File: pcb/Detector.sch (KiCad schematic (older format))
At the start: 13 parts, among them U3 AD8310

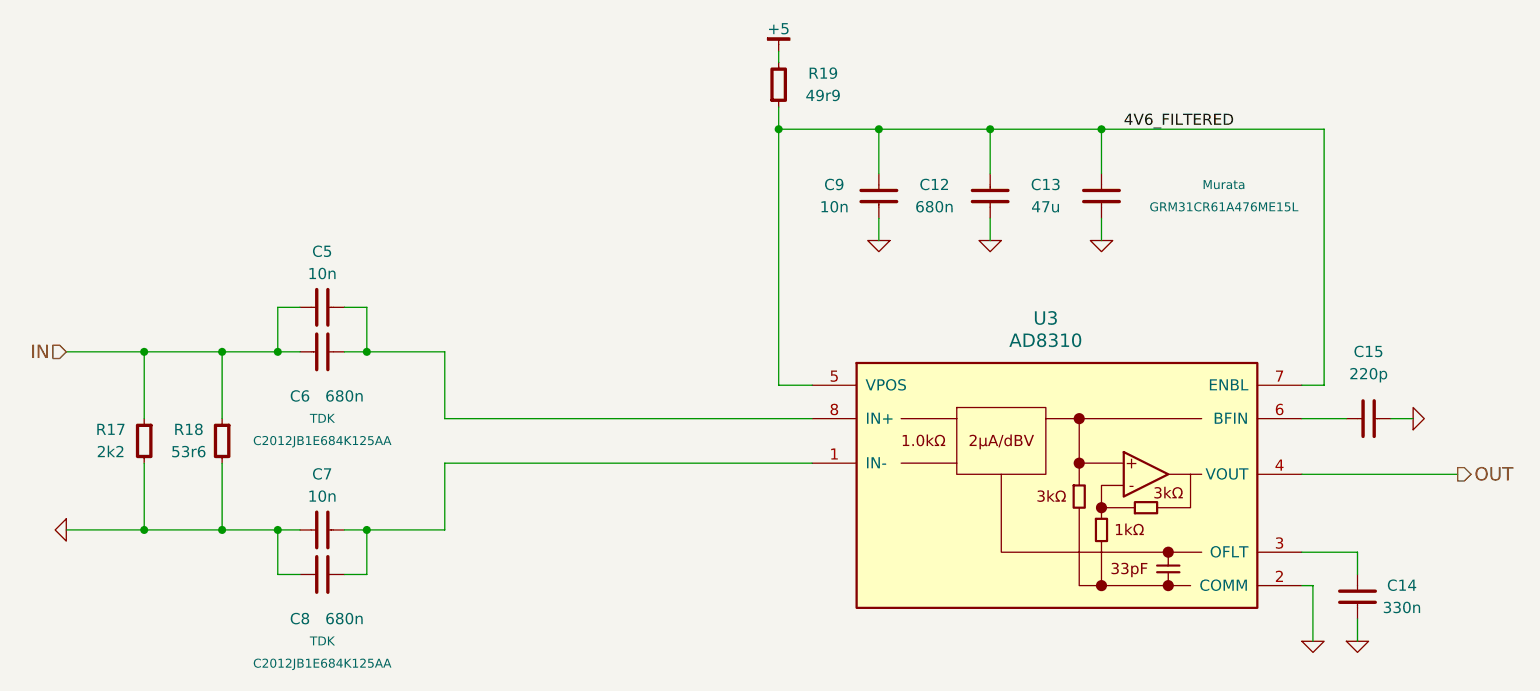
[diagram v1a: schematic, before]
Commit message: Specified part for C14
U# (AD8310) offset filter capacitor
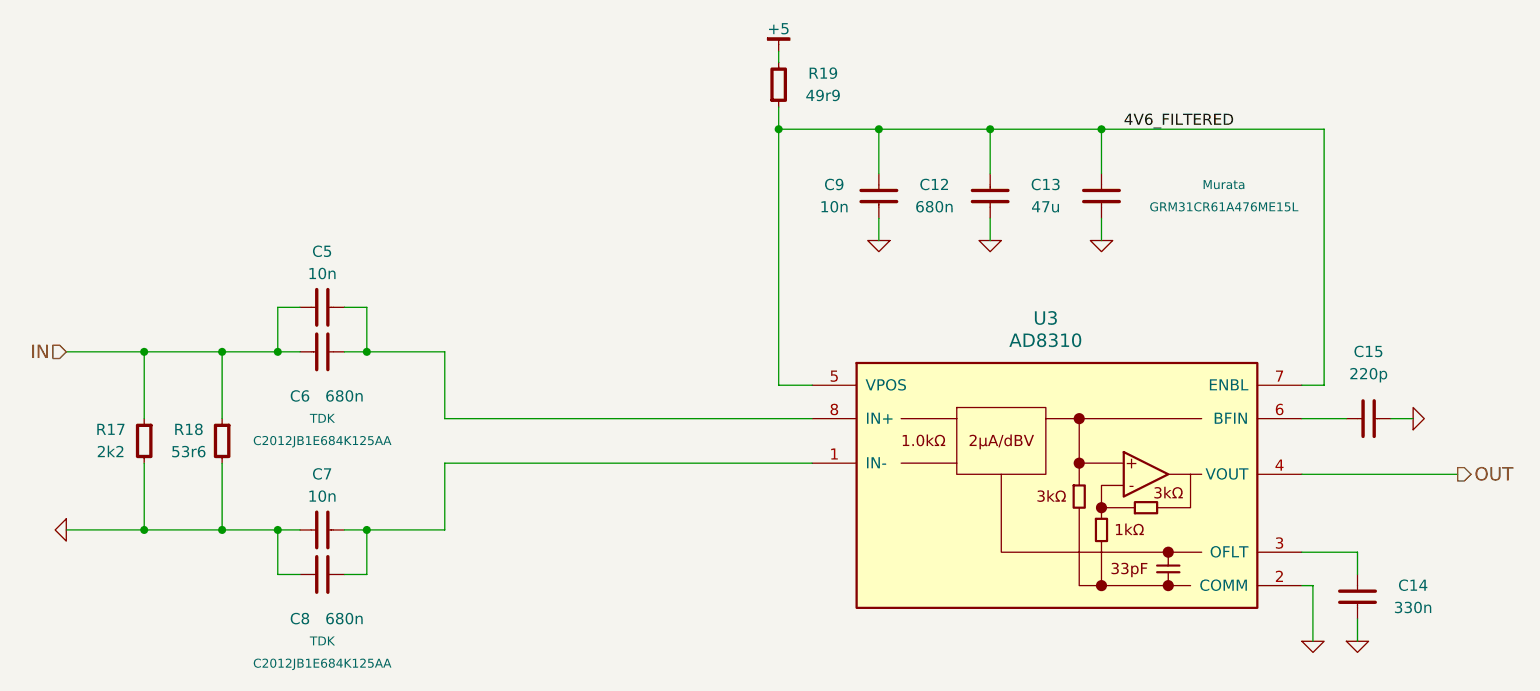
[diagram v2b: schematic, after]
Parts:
- removed C14: 330n, symbol C
- added C14: 330n, symbol C-0603
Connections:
- net GND: now also C14.2
- net at U3.3 (OFLT): now also C14.1
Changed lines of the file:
@@
-$EndComp
-$Comp
-L C C14
-U 1 1 545ED71F
-P 8350 4800
-F 0 "C14" H 8550 4850 50  0000 C CNN
-F 1 "330n" H 8550 4750 50  0000 C CNN
-F 2 "" H 8340 4775 60  0000 C CNN
-F 3 "" H 8340 4775 60  0000 C CNN
-	1    8350 4800
-	1    0    0    -1
 $EndComp
 $Comp
@@
 $EndComp
 $Comp
-L GND #PWR41
+L GND #PWR036
 U 1 1 545ED74D
 P 8150 5000
-F 0 "#PWR41" H 8150 5000 30  0001 C CNN
+F 0 "#PWR036" H 8150 5000 30  0001 C CNN
 F 1 "GND" H 8150 4930 30  0001 C CNN
 F 2 "" H 8150 5000 60  0000 C CNN
@@
 $EndComp
 $Comp
-L GND #PWR42
+L GND #PWR037
 U 1 1 545ED753
 P 8350 5000
-F 0 "#PWR42" H 8350 5000 30  0001 C CNN
+F 0 "#PWR037" H 8350 5000 30  0001 C CNN
 F 1 "GND" H 8350 4930 30  0001 C CNN
 F 2 "" H 8350 5000 60  0000 C CNN
@@
 $EndComp
 $Comp
-L GND #PWR43
+L GND #PWR038
 U 1 1 545ED759
 P 8600 4000
-F 0 "#PWR43" H 8600 4000 30  0001 C CNN
+F 0 "#PWR038" H 8600 4000 30  0001 C CNN
 F 1 "GND" H 8600 3930 30  0001 C CNN
 F 2 "" H 8600 4000 60  0000 C CNN
@@
 	3600 3500 3500 3500
 Wire Wire Line
-	3500 3700 3500 3500
+	3500 3500 3500 3700
 Connection ~ 3500 3700
 Wire Wire Line
@@
 Connection ~ 6700 2700
 $Comp
-L GND #PWR38
+L GND #PWR039
 U 1 1 545ED79D
 P 6200 3200
-F 0 "#PWR38" H 6200 3200 30  0001 C CNN
+F 0 "#PWR039" H 6200 3200 30  0001 C CNN
 F 1 "GND" H 6200 3130 30  0001 C CNN
 F 2 "" H 6200 3200 60  0000 C CNN
@@
 	6200 3200 6200 3100
 $Comp
-L GND #PWR39
+L GND #PWR040
 U 1 1 545ED7A4
 P 6700 3200
-F 0 "#PWR39" H 6700 3200 30  0001 C CNN
+F 0 "#PWR040" H 6700 3200 30  0001 C CNN
 F 1 "GND" H 6700 3130 30  0001 C CNN
 F 2 "" H 6700 3200 60  0000 C CNN
@@
 $EndComp
 $Comp
-L GND #PWR40
+L GND #PWR041
 U 1 1 545ED7C0
 P 7200 3200
-F 0 "#PWR40" H 7200 3200 30  0001 C CNN
+F 0 "#PWR041" H 7200 3200 30  0001 C CNN
 F 1 "GND" H 7200 3130 30  0001 C CNN
 F 2 "" H 7200 3200 60  0000 C CNN
@@
 	2550 4500 3600 4500
 $Comp
-L GND #PWR36
+L GND #PWR042
 U 1 1 545ED89C
 P 2550 4500
-F 0 "#PWR36" H 2550 4500 30  0001 C CNN
+F 0 "#PWR042" H 2550 4500 30  0001 C CNN
 F 1 "GND" H 2550 4430 30  0001 C CNN
 F 2 "" H 2550 4500 60  0000 C CNN
@@
 IN
 $Comp
-L +5 #PWR37
+L +5 #PWR043
 U 1 1 545EDBEE
 P 5750 2350
-F 0 "#PWR37" H 5750 2400 30  0001 C CNN
+F 0 "#PWR043" H 5750 2400 30  0001 C CNN
 F 1 "+5" H 5750 2450 50  0000 C CNN
 F 2 "" H 5750 2350 60  0000 C CNN
@@
 Wire Wire Line
 	4250 4000 4250 3700
+$Comp
+L C-0603 C14
+U 1 1 545FC255
+P 8350 4800
+F 0 "C14" H 8600 4850 50  0000 C CNN
+F 1 "330n" H 8600 4750 50  0000 C CNN
+F 2 "" H 8340 4775 60  0000 C CNN
+F 3 "" H 8340 4775 60  0000 C CNN
+F 4 "C1608JB1E334K080AC" H 8350 4800 60  0001 C CNN "PN"
+F 5 "TDK" H 8350 4800 60  0001 C CNN "Manuf"
+	1    8350 4800
+	1    0    0    -1
+$EndComp
 $EndSCHEMATC

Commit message: Associated parts with footprints
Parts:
- C12, C6, C8: footprint (none) -> IPC7351-Nominal:CAPC2012X70
- C13: footprint (none) -> IPC7351-Nominal:CAPC3216X70
- C14, C15: footprint (none) -> IPC7351-Nominal:CAPC1608X55
- C5, C7, C9: footprint (none) -> IPC7351-Nominal:CAPC1005X55
- R17, R18, R19: footprint (none) -> IPC7351-Nominal:RESC1005X40
- U3: footprint (none) -> IPC7351-Nominal:SOP65P490X109-8
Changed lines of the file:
@@
 F 0 "U3" H 6950 4950 60  0000 C CNN
 F 1 "AD8310" H 6950 4850 60  0000 C CNN
-F 2 "" H 7050 4400 60  0000 C CNN
+F 2 "IPC7351-Nominal:SOP65P490X109-8" H 7050 4400 60  0001 C CNN
 F 3 "" H 7050 4400 60  0000 C CNN
 	1    6950 4250
@@
 F 0 "C15" V 8700 4000 50  0000 C CNN
 F 1 "220p" V 8600 4000 50  0000 C CNN
-F 2 "" H 8390 3975 60  0000 C CNN
+F 2 "IPC7351-Nominal:CAPC1608X55" H 8390 3975 60  0001 C CNN
 F 3 "" H 8390 3975 60  0000 C CNN
 	1    8400 4000
@@
 F 0 "C6" V 3900 3600 50  0000 C CNN
 F 1 "680n" V 3900 3800 50  0000 C CNN
-F 2 "" H 3690 3675 60  0000 C CNN
+F 2 "IPC7351-Nominal:CAPC2012X70" H 3690 3675 60  0001 C CNN
 F 3 "" H 3690 3675 60  0000 C CNN
 F 4 "C2012JB1E684K125AA" V 4100 3700 40  0000 C CNN "PN"
@@
 F 0 "C5" V 3950 3500 50  0000 C CNN
 F 1 "10n" V 3850 3500 50  0000 C CNN
-F 2 "" H 3690 3475 60  0000 C CNN
+F 2 "IPC7351-Nominal:CAPC1005X55" H 3690 3475 60  0001 C CNN
 F 3 "" H 3690 3475 60  0000 C CNN
 	1    3700 3500
@@
 F 0 "C8" V 3900 4600 50  0000 C CNN
 F 1 "680n" V 3900 4800 50  0000 C CNN
-F 2 "" H 3690 4675 60  0000 C CNN
+F 2 "IPC7351-Nominal:CAPC2012X70" H 3690 4675 60  0001 C CNN
 F 3 "" H 3690 4675 60  0000 C CNN
 F 4 "C2012JB1E684K125AA" V 4100 4700 40  0000 C CNN "PN"
@@
 F 0 "C7" V 3950 4500 50  0000 C CNN
 F 1 "10n" V 3850 4500 50  0000 C CNN
-F 2 "" H 3690 4475 60  0000 C CNN
+F 2 "IPC7351-Nominal:CAPC1005X55" H 3690 4475 60  0001 C CNN
 F 3 "" H 3690 4475 60  0000 C CNN
 	1    3700 4500
@@
 F 0 "R18" H 3400 4150 50  0000 C CNN
 F 1 "53r6" H 3400 4050 50  0000 C CNN
-F 2 "" H 3250 4150 60  0000 C CNN
+F 2 "IPC7351-Nominal:RESC1005X40" H 3250 4150 60  0001 C CNN
 F 3 "" H 3250 4150 60  0000 C CNN
 	1    3250 4100
@@
 F 0 "R19" H 5950 2450 50  0000 C CNN
 F 1 "49r9" H 5950 2550 50  0000 C CNN
-F 2 "" H 5750 2550 60  0000 C CNN
+F 2 "IPC7351-Nominal:RESC1005X40" H 5750 2550 60  0001 C CNN
 F 3 "" H 5750 2550 60  0000 C CNN
 	1    5750 2500
@@
 F 0 "C12" H 6450 2950 50  0000 C CNN
 F 1 "680n" H 6450 3050 50  0000 C CNN
-F 2 "" H 6690 2975 60  0000 C CNN
+F 2 "IPC7351-Nominal:CAPC2012X70" H 6690 2975 60  0001 C CNN
 F 3 "" H 6690 2975 60  0000 C CNN
 F 4 "C2012JB1E684K125AA" V 7100 3000 40  0001 C CNN "PN"
@@
 F 0 "C9" H 6400 3050 50  0000 C CNN
 F 1 "10n" H 6400 2950 50  0000 C CNN
-F 2 "" H 6190 2975 60  0000 C CNN
+F 2 "IPC7351-Nominal:CAPC1005X55" H 6190 2975 60  0001 C CNN
 F 3 "" H 6190 2975 60  0000 C CNN
 	1    6200 3000
@@
 F 0 "R17" H 3050 4150 50  0000 C CNN
 F 1 "2k2" H 3050 4050 50  0000 C CNN
-F 2 "" H 2900 4150 60  0000 C CNN
+F 2 "IPC7351-Nominal:RESC1005X40" H 2900 4150 60  0001 C CNN
 F 3 "" H 2900 4150 60  0000 C CNN
 	1    2900 4100
@@
 F 0 "C13" H 7450 3050 50  0000 C CNN
 F 1 "47u" H 7450 2950 50  0000 C CNN
-F 2 "" H 7190 2975 60  0000 C CNN
+F 2 "IPC7351-Nominal:CAPC3216X70" H 7190 2975 60  0001 C CNN
 F 3 "" H 7190 2975 60  0000 C CNN
 F 4 "GRM31CR61A476ME15L" H 6650 2950 40  0000 C CNN "PN"
@@
 F 0 "C14" H 8600 4850 50  0000 C CNN
 F 1 "330n" H 8600 4750 50  0000 C CNN
-F 2 "" H 8340 4775 60  0000 C CNN
+F 2 "IPC7351-Nominal:CAPC1608X55" H 8340 4775 60  0001 C CNN
 F 3 "" H 8340 4775 60  0000 C CNN
 F 4 "C1608JB1E334K080AC" H 8350 4800 60  0001 C CNN "PN"
